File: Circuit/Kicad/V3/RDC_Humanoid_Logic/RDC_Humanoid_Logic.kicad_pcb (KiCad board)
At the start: 2 copper layers, 157 x 137 mm, 70 parts, among them J1 XT60, J2 Conn_01x03, J3 Conn_01x03, J4 Raspi_connect, Q1 Q_PMOS_GDS, Q2 Q_PMOS_GDS, SW1 SW_SPDT, SW2 SW_SPDT, SW3 SW_SPDT, U1 ISOW1044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

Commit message: 修正箇所を修正した
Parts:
- added J5: 74AHC1G04W5, Package_TO_SOT_SMD:SOT-23-5, F.Cu at (43.0, 27.6)
- added J6: CH213K, Package_TO_SOT_SMD:SOT-23-3, F.Cu at (179.6, 114.4)
- added J7: CH213K, Package_TO_SOT_SMD:SOT-23-3, F.Cu at (196.5, 114.5)
- added U4: TBD62083AFG, Package_SO:SOP-18_7.495x11.515mm_P1.27mm, F.Cu at (46.8, 18.6)
- moved H3 219.2 mm to (268.0, 61.7)
- moved H1 198.4 mm to (268.0, 51.3)
- moved H4 112.2 mm to (279.0, 61.8)
- moved H2 62.6 mm to (279.0, 51.5)
- moved D2 16.5 mm to (114.0, 26.5)
- moved D3 16.5 mm to (125.1, 26.4)
- moved R11 16.5 mm to (119.4, 28.0)
- moved R10 16.5 mm to (125.1, 27.9)
- moved R9 16.5 mm to (114.0, 28.0)
- moved D4 16.5 mm to (119.5, 26.5)
- moved SW1 4.77 mm to (130.8, 31.7)
- moved SW2 4.77 mm to (136.3, 31.7)
- moved SW3 4.77 mm to (141.8, 31.8)
- moved D5 2.28 mm to (136.0, 42.0)
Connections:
- FB2 pad 1: +5V -> Net-(J6-Pin_2)
- FB3 pad 1: +5V -> Net-(J6-Pin_2)
- FB7 pad 1: +5V -> Net-(J7-Pin_2)
- FB8 pad 1: +5V -> Net-(J7-Pin_2)
- J4 pad 1: unconnected-(J4-Pin_1-Pad1) -> EN_STM_VCC
- R3 pad 1: +5V -> Net-(J6-Pin_2)
- R5 pad 1: +5V -> Net-(J7-Pin_2)
- R7 pad 1: Net-(D5-K) -> Net-(J5-Pin_4)
- R8 pad 1: Net-(SW3-C) -> Net-(SW3-A)
- SW2 pad 1: unconnected-(SW2-A-Pad1) -> Net-(J5-Pin_4)
- SW2 pad 3: Net-(D5-K) -> unconnected-(SW2-C-Pad3)
- SW3 pad 1: unconnected-(SW3-A-Pad1) -> Net-(SW3-A)
- SW3 pad 3: Net-(SW3-C) -> unconnected-(SW3-C-Pad3)
- U3 pad 48: /CAN_Trans1/CAN_TX -> /CAN_Trans1/CAN_RX
- U3 pad 50: /CAN_Trans1/CAN_RX -> /CAN_Trans1/CAN_TX
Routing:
- net +5V: track 177.4 -> 91.8 mm, vias 8 -> 3
- net Net-(J6-Pin_2): track 0.00 -> 30.3 mm, vias 0 -> 2
- net Net-(J7-Pin_2): track 0.00 -> 30.2 mm, vias 0 -> 2
- net unconnected-(SW3-C-Pad3): track 0.00 -> 20.6 mm
- net Net-(SW3-C): track 38.2 -> 22.4 mm, vias 2 -> 0
- net RasPi_Power: track 50.7 -> 38.3 mm, vias 2 -> 0
- net GND: track 26.8 -> 29.7 mm, vias 270 -> 2
- net Net-(D5-K): track 49.8 -> 47.2 mm, vias 2 -> 1
- net EN_STM: track 43.3 -> 45.4 mm, vias 2 -> 0
- net Net-(SW1-B): track 65.5 -> 63.7 mm, vias 4 -> 0
- net Logic_Power: track 63.1 -> 64.7 mm, vias 2 -> 0
- net Net-(U2-V_{ISOIN}): vias 2 -> 0
- net Net-(U1-V_{ISOIN}): vias 2 -> 0
- net GND1: vias 39 -> 0
- net /Logic_Power/EN_STM_Power: vias 2 -> 0
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- removed copper zone on B.Cu, net GND
- removed copper zone on F.Cu, net GND
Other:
- board outline removed

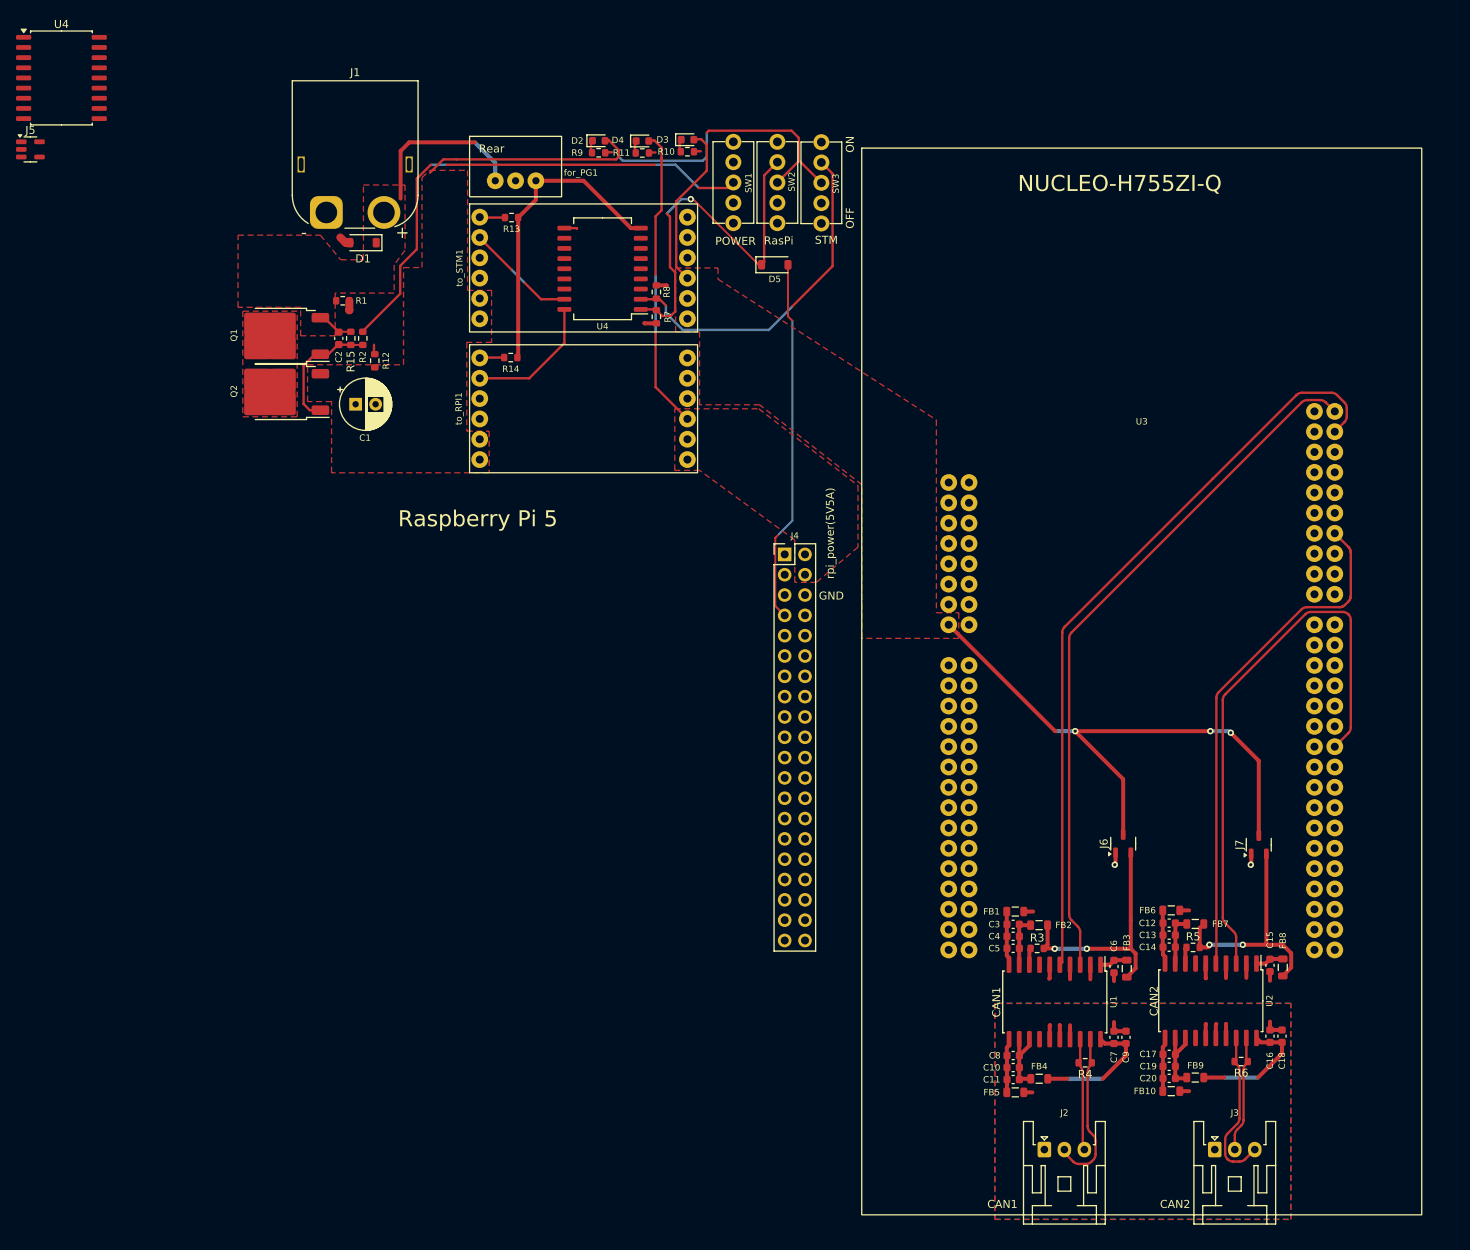
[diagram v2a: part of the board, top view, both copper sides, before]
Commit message: Update V3 logic. 回路図の更新完了。PCB途中
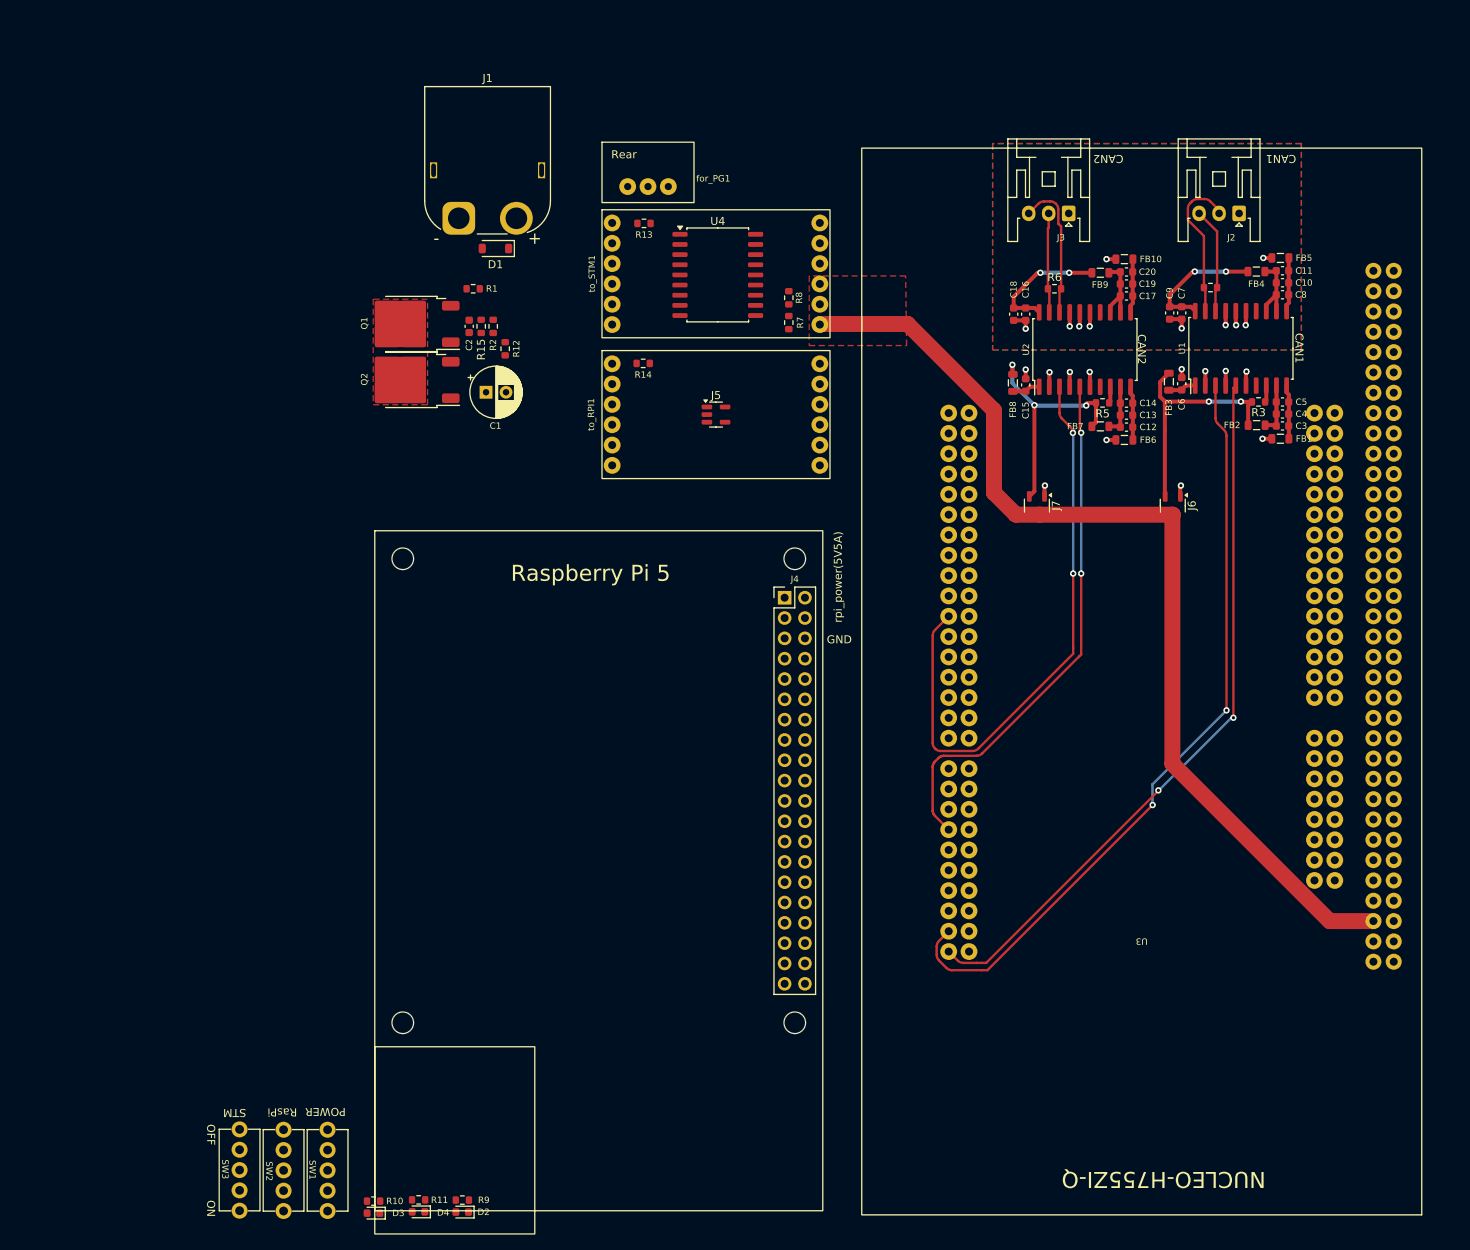
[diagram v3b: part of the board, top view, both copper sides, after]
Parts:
- removed D5: D, Diode_SMD:D_SOD-123
- removed the U4 at (114.5, 42.5)
- moved SW3 143.2 mm to (69.1, 155.2), turned to -90 degrees
- moved D3 139.8 mm to (85.8, 160.5), turned to 180 degrees
- moved SW2 138.1 mm to (74.6, 155.2), turned to -90 degrees
- moved R10 136.9 mm to (85.8, 159.0), turned to 180 degrees
- moved D4 136.8 mm to (91.5, 160.4), turned to 180 degrees
- moved D2 135.0 mm to (96.9, 160.4), turned to 180 degrees
- moved R11 133.8 mm to (91.5, 158.9), turned to 180 degrees
- moved SW1 133.5 mm to (80.1, 155.2), turned to -90 degrees
- moved R9 132.0 mm to (96.9, 158.9), turned to 180 degrees
- moved J2 119.5 mm to (194.0, 35.6), turned to 180 degrees
- moved J3 118.4 mm to (172.7, 35.6), turned to 180 degrees
- moved FB5 109.4 mm to (199.2, 41.1), turned to 180 degrees
- moved C11 106.6 mm to (199.5, 42.8), turned to 0 degrees
- moved FB4 104.5 mm to (196.2, 42.9), turned to 180 degrees
- moved FB10 104.2 mm to (179.7, 41.3), turned to 180 degrees
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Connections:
- U3 pad 15: +5V -> unconnected-(U3-VIN-Pad15)
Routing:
- net Logic_Power: track 64.7 -> 0.00 mm
- net Net-(SW1-B): track 63.7 -> 0.00 mm
- net Net-(D5-K): track 47.2 -> 0.00 mm, vias 1 -> 0
- net EN_STM: track 45.4 -> 0.00 mm
- net EN_Power: track 38.6 -> 0.00 mm
- net RasPi_Power: track 38.3 -> 0.00 mm
- net +5V: track 91.8 -> 124.9 mm, vias 3 -> 0
- net +12V: track 26.1 -> 0.00 mm
- net Net-(SW3-C): track 22.4 -> 0.00 mm
- net unconnected-(SW3-C-Pad3): track 20.6 -> 0.00 mm
- net /Logic_Power/EN_RasPi_Power: track 16.6 -> 0.00 mm
- net Net-(Q1-G): track 15.6 -> 0.00 mm
- net /Logic_Power/EN_STM_Power: track 13.8 -> 0.00 mm
- net GND: track 29.7 -> 18.5 mm, vias 2 -> 12
- net /CAN_Trans1/CAN_TX: track 87.5 -> 97.0 mm, vias 0 -> 2
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- removed copper zone on F.Cu, net +12V
- removed copper zone on F.Cu, net Logic_Power
- removed copper zone on F.Cu, net RasPi_Power

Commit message: 配線途中
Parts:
- moved J2 118.6 mm to (171.2, 152.0), turned to 0 degrees
- moved J3 118.1 mm to (192.5, 152.0), turned to 0 degrees
- moved FB5 111.3 mm to (166.0, 147.4), turned to 0 degrees
- moved C11 108.4 mm to (165.8, 145.8), turned to 180 degrees
- moved FB4 106.4 mm to (169.0, 145.7), turned to 0 degrees
- moved FB10 106.1 mm to (185.5, 147.2), turned to 0 degrees
- moved C10 105.6 mm to (165.8, 144.3), turned to 180 degrees
- moved FB9 103.2 mm to (188.5, 145.5), turned to 0 degrees
- moved C20 102.9 mm to (185.3, 145.6), turned to 180 degrees
- moved C8 102.7 mm to (165.8, 142.8), turned to 180 degrees
- moved R6 101.3 mm to (194.3, 143.5), turned to 180 degrees
- moved R4 100.1 mm to (174.8, 143.7), turned to 180 degrees
- moved C19 99.9 mm to (185.3, 144.1), turned to 180 degrees
- moved C18 98.1 mm to (199.4, 140.4), turned to 90 degrees
- moved C16 97.1 mm to (197.9, 140.4), turned to 90 degrees
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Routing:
- net /CAN_Trans1/CAN_RX: track 90.5 -> 25.6 mm, vias 2 -> 0
- net /CAN_Trans1/CAN_TX: track 97.0 -> 33.8 mm
- net /Logic_Power/EN_RasPi_Power: track 0.00 -> 24.2 mm, vias 0 -> 1
- net Net-(Q1-G): track 0.00 -> 14.8 mm
- net /Logic_Power/EN_STM_Power: track 0.00 -> 12.5 mm, vias 0 -> 1
- net Net-(J5-Pin_4): track 0.00 -> 11.8 mm
- net Net-(SW3-A): track 0.00 -> 9.77 mm
- net /CAN_Trans2/CAN_RX: track 66.7 -> 59.9 mm
- net Net-(J7-Pin_2): track 30.5 -> 24.9 mm
- net Net-(J6-Pin_2): track 30.3 -> 24.8 mm
- net /CAN_Trans2/CAN_TX: track 73.7 -> 69.4 mm
- net GND: track 18.5 -> 22.0 mm, vias 12 -> 15
- net /CAN_Trans1/CANH: track 19.2 -> 18.2 mm
- net /CAN_Trans1/CANL: track 13.4 -> 12.5 mm
- net /CAN_Trans2/CANH: track 13.1 -> 12.2 mm
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- added copper zone on F.Cu, net +12V
- added copper zone on F.Cu, net Logic_Power
- added copper zone on F.Cu, net RasPi_Power

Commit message: Logic V.3の完了
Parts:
- moved H4 233.9 mm to (61.5, 148.0)
- moved H2 194.0 mm to (86.0, 32.0)
- moved H3 107.0 mm to (221.5, 158.0)
- moved J5 92.7 mm to (76.5, 140.2), turned to -90 degrees
- moved H1 50.8 mm to (221.0, 32.0)
- moved R9 39.8 mm to (61.2, 155.2), turned to 90 degrees
- moved D2 39.8 mm to (61.2, 158.4), turned to -90 degrees
- moved R11 32.9 mm to (62.8, 155.2), turned to 90 degrees
- moved D4 32.8 mm to (62.8, 158.3), turned to -90 degrees
- moved R10 25.8 mm to (64.2, 155.2), turned to 90 degrees
- moved D3 25.7 mm to (64.2, 158.4), turned to -90 degrees
- moved R7 8.47 mm to (138.8, 43.8), turned to 0 degrees
- moved R8 6.88 mm to (138.8, 42.2), turned to 0 degrees
- moved J2 2.00 mm to (171.2, 154.0)
- moved J3 2.00 mm to (192.5, 154.0)
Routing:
- net +5V: track 124.9 -> 301.8 mm, vias 0 -> 2
- net Logic_Power: track 0.00 -> 137.9 mm, vias 0 -> 1
- net Net-(SW3-A): track 9.77 -> 141.1 mm
- net Net-(J5-Pin_4): track 11.8 -> 140.9 mm
- net RasPi_Power: track 0.00 -> 123.8 mm
- net Net-(SW1-B): track 0.00 -> 102.2 mm, vias 0 -> 1
- net EN_STM_VCC: track 0.00 -> 85.7 mm
- net EN_STM: track 0.00 -> 81.4 mm, vias 0 -> 1
- net EN_Power: track 0.08 -> 26.4 mm
- net GND: track 22.0 -> 38.8 mm, vias 15 -> 435
- net Net-(Q1-G): track 14.8 -> 8.51 mm
- net /Logic_Power/RasPi_PG: track 0.00 -> 3.08 mm
- net /Logic_Power/STM_PG: track 0.06 -> 3.11 mm
- net /CAN_Trans1/CANL: track 12.5 -> 14.5 mm
- net /CAN_Trans2/CANH: track 12.2 -> 14.2 mm
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- added copper zone on B.Cu, net GND
- added copper zone on F.Cu, net GND
- added copper zone on F.Cu, net Net-(Q1-G)
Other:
- board outline added: 168 x 134 mm
- board text added: "RDC_Bipedal_Robot - Circuit Name : Logic_Board - Version : 3.0 - Designed Date : 2025/07/29 - Designer Name - Yuya Mochizuki - Yusuke Yamasaki"
- board text added: "修正したい"
- board text removed: "OFF"
- board text removed: "ON"
- board text removed: "RDC_Bipedal_Robot - Circuit Name : Logic_Board - Version : 2.0 - Designed Date : 2025/03/11 - Designer Name - Yuya Mochizuki - Yusuke Yamasaki"
